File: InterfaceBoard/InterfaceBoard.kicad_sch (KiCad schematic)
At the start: 11 parts, among them J5 SPI, J6 RS232, J7 UART

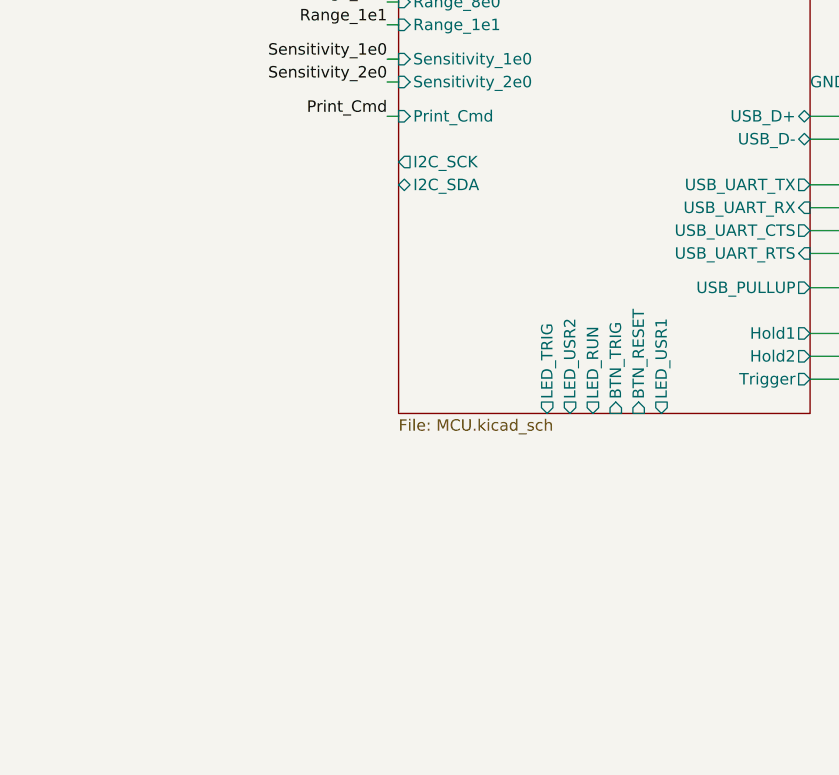
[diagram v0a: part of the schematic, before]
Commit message: InterfaceBoard: Place and route buttons and LEDs.
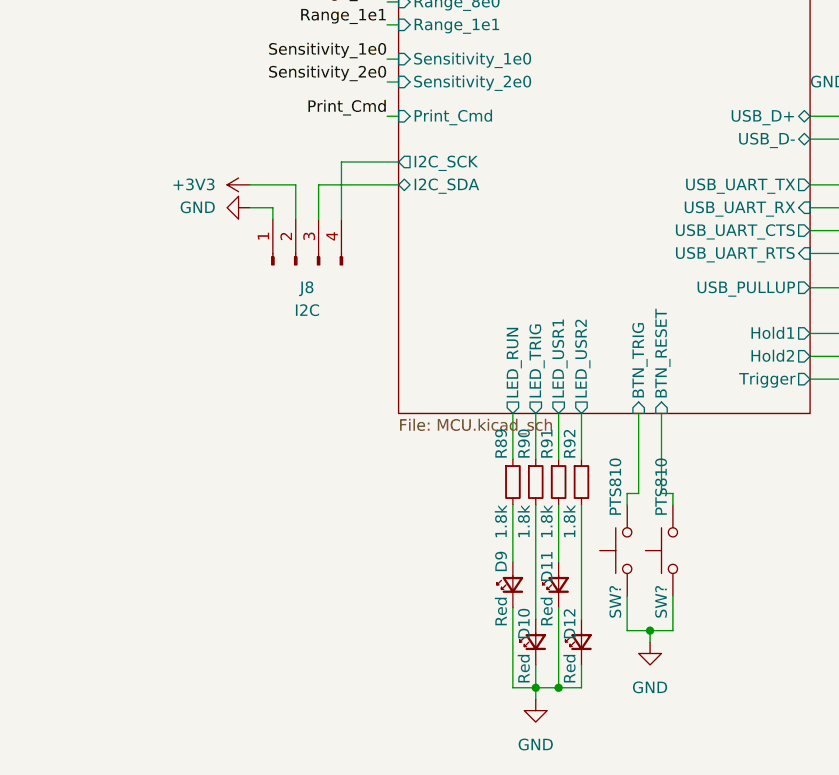
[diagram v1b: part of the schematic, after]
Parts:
- added D10, D11, D12, D9: Red, LED_SMD:LED_0603_1608Metric, symbol Device:LED_Small
- added J8: I2C, Connector_PinHeader_1.27mm:PinHeader_1x04_P1.27mm_Vertical, symbol Connector:Conn_01x04_Male
- added R89, R90, R91, R92: 1.8k, Resistor_SMD:R_0603_1608Metric, symbol Device:R_Small
- added SW? (x2): PTS810, Button_Switch_SMD:SW_SPST_PTS810, symbol Switch:SW_Push
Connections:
- net +3V3: now also J8.2 (Pin_2)
- net GND: now also D10.1 (K), D11.1 (K), D12.1 (K), D9.1 (K), J8.1 (Pin_1), SW?.1, SW?.1
- net MCU/BTN_RESET: now also SW?.2
- net MCU/BTN_TRIG: now also SW?.2
- net MCU/I2C_SCK: now also J8.4 (Pin_4)
- net MCU/I2C_SDA: now also J8.3 (Pin_3)
- net MCU/LED_RUN: now also R89.1
- net MCU/LED_TRIG: now also R90.1
- net MCU/LED_USR1: now also R91.1
- net MCU/LED_USR2: now also R92.1
- new net: D11.2 (A), R91.2
- new net: D9.2 (A), R89.2
- new net: D12.2 (A), R92.2
- new net: D10.2 (A), R90.2

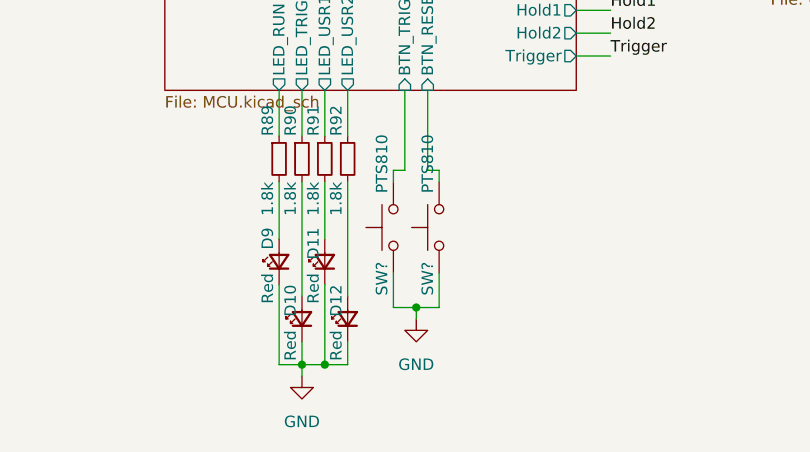
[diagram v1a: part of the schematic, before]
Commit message: InterfaceBoard: Route MCU USB
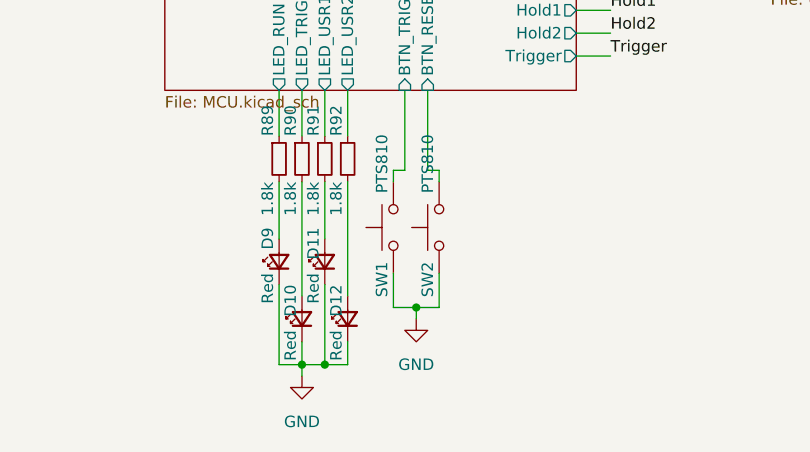
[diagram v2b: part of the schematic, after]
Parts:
- gave numbers to parts that had none: 2
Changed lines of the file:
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@@
   (symbol (lib_id "power:GND") (at 166.37 168.91 0) (unit 1)
     (in_bom yes) (on_board yes) (fields_autoplaced)
-    (property "Reference" "#PWR?" (id 0) (at 166.37 175.26 0)
+    (property "Reference" "#PWR0192" (id 0) (at 166.37 175.26 0)
       (effects (font (size 1.27 1.27)) hide)
     )
@@
   (symbol (lib_id "Switch:SW_Push") (at 168.91 158.75 90) (unit 1)
     (in_bom yes) (on_board yes)
-    (property "Reference" "SW?" (id 0) (at 167.64 162.56 0)
+    (property "Reference" "SW2" (id 0) (at 167.64 162.56 0)
       (effects (font (size 1.27 1.27)) (justify right))
     )
@@
   (symbol (lib_id "Switch:SW_Push") (at 163.83 158.75 90) (unit 1)
     (in_bom yes) (on_board yes)
-    (property "Reference" "SW?" (id 0) (at 162.56 162.56 0)
+    (property "Reference" "SW1" (id 0) (at 162.56 162.56 0)
       (effects (font (size 1.27 1.27)) (justify right))
     )
@@
     )
     (path "/34c2389e-7cc3-4011-a4b7-c500c338b4f5"
-      (reference "#PWR?") (unit 1) (value "GND") (footprint "")
+      (reference "#PWR0192") (unit 1) (value "GND") (footprint "")
     )
     (path "/7510d84d-561c-4c04-9a47-602785bf143f/33265ba7-ef1d-49c8-b2f9-33fbd5dfa7c1"
@@
     )
     (path "/d74a2181-f350-48db-a6ce-51542911d227/a7baf01e-0c76-439f-b122-e367567d3ea6"
-      (reference "R17") (unit 1) (value "27R") (footprint "Resistor_SMD:R_0603_1608Metric")
+      (reference "R17") (unit 1) (value "27") (footprint "Resistor_SMD:R_0603_1608Metric")
     )
     (path "/d74a2181-f350-48db-a6ce-51542911d227/d3d68b99-08a5-4c99-9a33-446706bf67f9"
-      (reference "R18") (unit 1) (value "27R") (footprint "Resistor_SMD:R_0603_1608Metric")
+      (reference "R18") (unit 1) (value "27") (footprint "Resistor_SMD:R_0603_1608Metric")
     )
     (path "/d74a2181-f350-48db-a6ce-51542911d227/93fd99b4-a7d1-4c0a-9383-1aa421c4f961"
-      (reference "R19") (unit 1) (value "27R") (footprint "Resistor_SMD:R_0603_1608Metric")
+      (reference "R19") (unit 1) (value "27") (footprint "Resistor_SMD:R_0603_1608Metric")
     )
     (path "/d74a2181-f350-48db-a6ce-51542911d227/d1bc8c3d-57af-4327-afee-9ed00b7b0341"
-      (reference "R20") (unit 1) (value "27R") (footprint "Resistor_SMD:R_0603_1608Metric")
+      (reference "R20") (unit 1) (value "27") (footprint "Resistor_SMD:R_0603_1608Metric")
     )
     (path "/d74a2181-f350-48db-a6ce-51542911d227/44246ea6-1314-49f4-810f-a437a22916fd"
@@
       (reference "R92") (unit 1) (value "1.8k") (footprint "Resistor_SMD:R_0603_1608Metric")
     )
+    (path "/d74a2181-f350-48db-a6ce-51542911d227/e38c6fa7-6a25-4264-bcbb-da4e3cff0be7"
+      (reference "R93") (unit 1) (value "0") (footprint "Resistor_SMD:R_0603_1608Metric")
+    )
+    (path "/d74a2181-f350-48db-a6ce-51542911d227/f6648d5d-2b98-4a44-aa90-a29b5a2c0a10"
+      (reference "R94") (unit 1) (value "0") (footprint "Resistor_SMD:R_0603_1608Metric")
+    )
+    (path "/fa5be8f7-51b3-41aa-b87c-301c3f8efc33"
+      (reference "SW1") (unit 1) (value "PTS810") (footprint "Button_Switch_SMD:SW_SPST_PTS810")
+    )
     (path "/c6c0c2db-0b52-4029-bffa-d55f68440e63"
-      (reference "SW?") (unit 1) (value "PTS810") (footprint "Button_Switch_SMD:SW_SPST_PTS810")
-    )
-    (path "/fa5be8f7-51b3-41aa-b87c-301c3f8efc33"
-      (reference "SW?") (unit 1) (value "PTS810") (footprint "Button_Switch_SMD:SW_SPST_PTS810")
+      (reference "SW2") (unit 1) (value "PTS810") (footprint "Button_Switch_SMD:SW_SPST_PTS810")
     )
     (path "/6b1005e4-cf6f-4a1d-aca2-678196de2d73"

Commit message: InterfaceBoard: Rev 1.0
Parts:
- renumbered D11 to D5, D12 to D6, D9 to D7, D10 to D8, H4 to H1, H1 to H4, J5 to J1, J8 to J2, J7 to J6, J6 to J8, R91 to R51, R92 to R52, R89 to R53, R90 to R54, TP7 to TP5
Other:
- company: (none) -> Peter Farley
- title: (none) -> Kiethley 615 Interface Board

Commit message: InterfaceBoard: Add BOM
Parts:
- D5, D6, D7, D8: DigiKey (none) -> https://www.digikey.com/en/products/detail/harvatek-corpora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
- H1, H2, H3, H4, J6, J8: now left out of the parts list
- R51, R52, R53, R54: DigiKey https://www.digikey.com/ordering/shoppingcart -> https://www.digikey.com/en/products/detail/stackpole-electr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
- SW1, SW2: DigiKey (none) -> https://www.digikey.com/en/products/detail/c-k/PTS810-SJK-2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
